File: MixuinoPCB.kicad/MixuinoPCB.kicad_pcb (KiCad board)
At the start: 2 copper layers, 83.8 x 81.3 mm, 13 parts

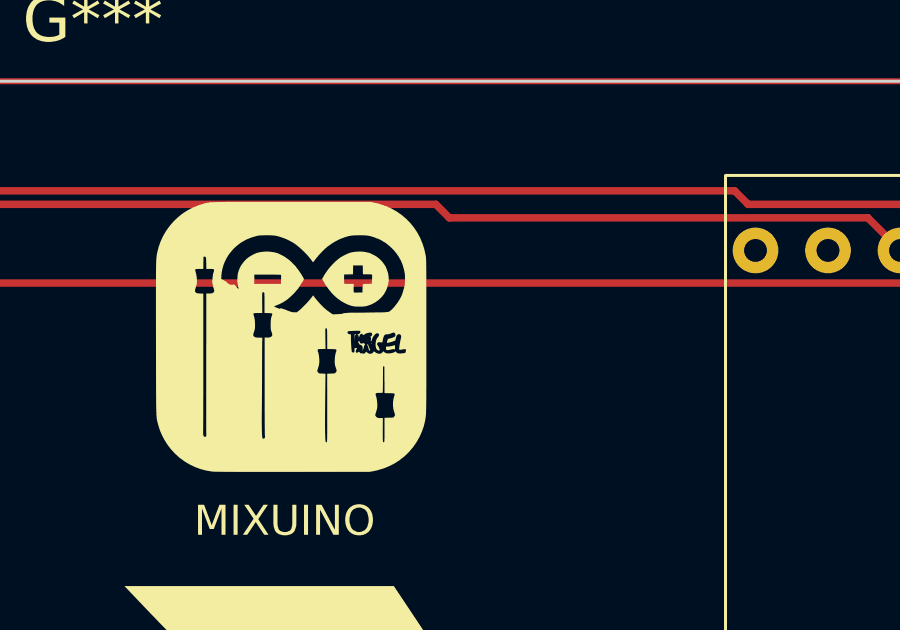
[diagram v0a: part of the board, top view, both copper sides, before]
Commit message: Added some credit to the pcb
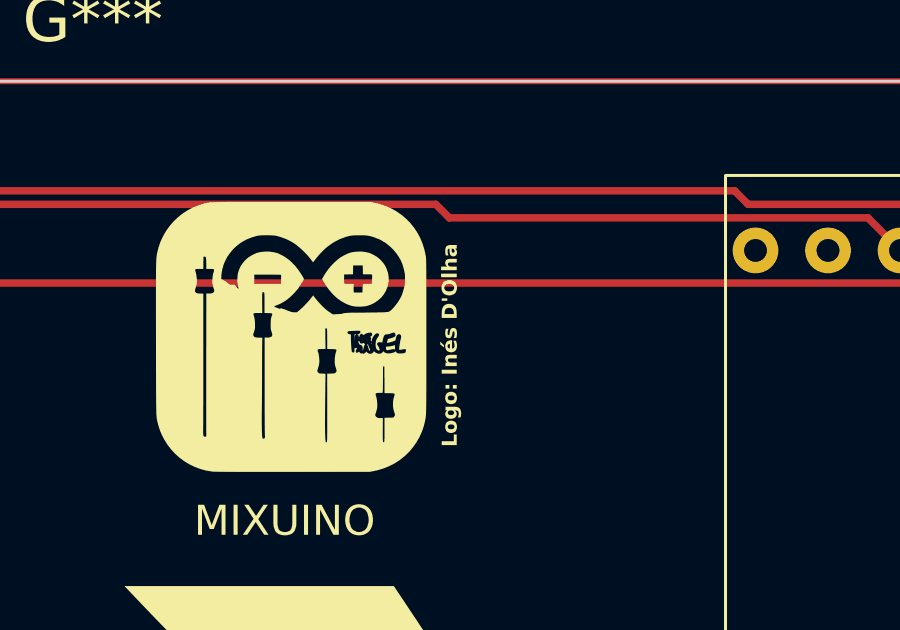
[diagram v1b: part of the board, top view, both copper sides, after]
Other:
- board text added: "Logo: Inés D'Olha"
